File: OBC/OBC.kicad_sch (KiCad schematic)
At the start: 15 parts, among them J101 Modos de operación, J102 PMS-Raspi, J103 Conector UART, J104 Raspi-TRU, U101 RASPBERRY_PI_ZERO_2_W, U102 BMP280, U103 MPU9250

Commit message: Propone disposicion pcb
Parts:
- J103: footprint Connector_JST:JST_XH_S3B-XH-A-1_1x03_P2.50mm_Horizontal -> Connector_PinHeader_2.54mm:PinHeader_1x03_P2.54mm_Vertical
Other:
- sheet ADS1115_ADC ports: added +3.3v; removed +5V
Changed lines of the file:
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@@
 			)
 		)
-		(property "Footprint" "Connector_JST:JST_XH_S3B-XH-A-1_1x03_P2.50mm_Horizontal"
+		(property "Footprint" "Connector_PinHeader_2.54mm:PinHeader_1x03_P2.54mm_Vertical"
 			(at 245.11 107.95 0)
 			(effects
@@
 			)
 		)
-		(pin "+5V" input
+		(pin "+3.3v" input
 			(at 240.03 55.88 180)
 			(effects

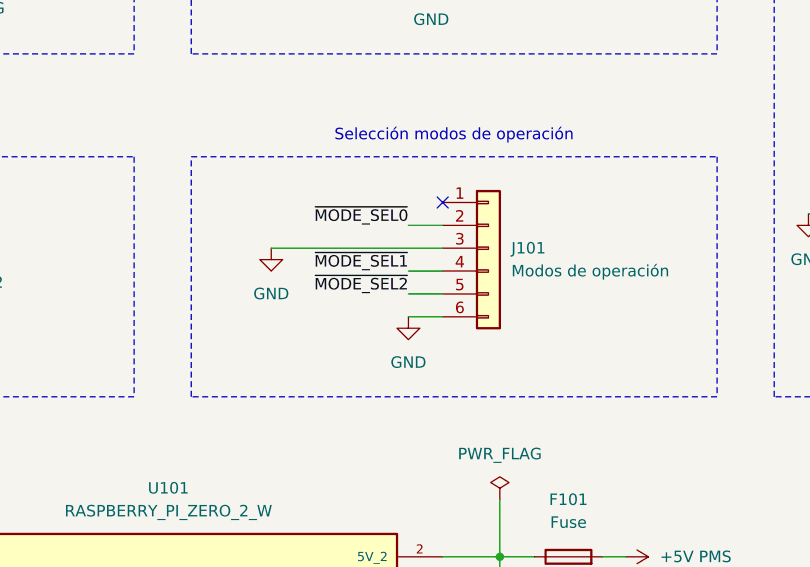
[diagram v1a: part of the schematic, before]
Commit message: Cambia disposición del selector de modos
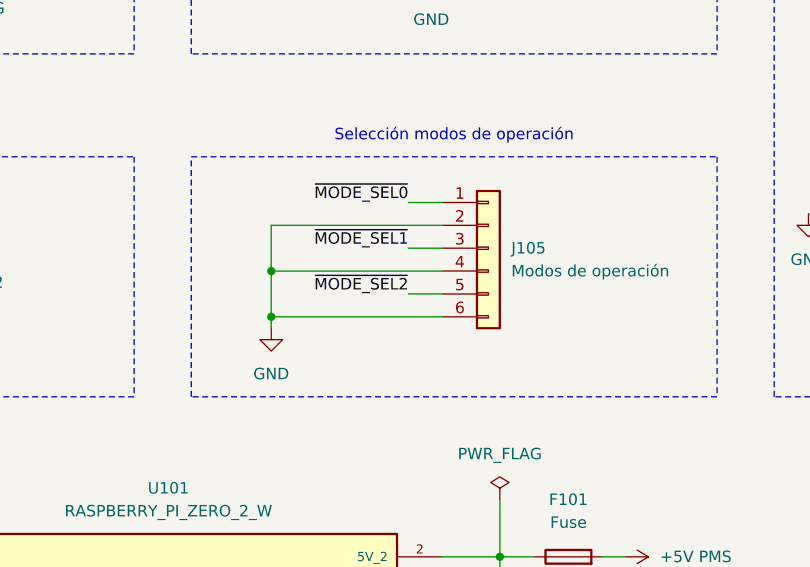
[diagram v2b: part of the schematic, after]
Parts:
- removed J101: Modos de operación, Connector_JST:JST_XH_S6B-XH-A_1x06_P2.50mm_Horizontal, symbol Connector_Generic:Conn_01x06
- added J105: Modos de operación, Connector_JST:JST_XH_S6B-XH-A_1x06_P2.50mm_Horizontal, symbol Connector_Generic:Conn_01x06
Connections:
- net GND: now also J105.2 (Pin_2), J105.4 (Pin_4), J105.6 (Pin_6)
- net ~{MODE_SEL0}: now also J105.1 (Pin_1)
- net ~{MODE_SEL1}: now also J105.3 (Pin_3)
- net ~{MODE_SEL2}: now also J105.5 (Pin_5)
- no-connect marks 38 -> 37

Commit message: Revisión v1.0
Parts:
- removed R106: 10k, Resistor_SMD:R_0603_1608Metric, symbol Device:R_Small
- R103, R104, R105: value 10k -> R
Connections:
- net +5V PMS: now also J104.6 (Pin_6); no longer J104.5 (Pin_5)
- net GND: now also U101.14 (GND_14), U101.20 (GND_20), U101.25 (GND_25), U101.30 (GND_30), U101.34 (GND_34), U101.39 (GND_39), U101.9 (GND_9); no longer J104.6 (Pin_6)
- net ~{MODE_SEL0}: now also J105.5 (Pin_5); no longer J105.1 (Pin_1)
- net ~{MODE_SEL2}: now also J105.1 (Pin_1); no longer J105.5 (Pin_5)
- net at C101.1, F101.1, U101.2 (5V_2): now also U101.4 (5V_4)
- net AIN3: no longer names the net of J104.4 (Pin_4)
- no-connect marks 37 -> 32
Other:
- company: (none) -> Team Corex
- title: (none) -> On Board Computer

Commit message: Correcciones menores
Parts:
- renumbered J102 to J101, J104 to J102, J105 to J103, J103 to J104, R105 to R101, R103 to R102, R104 to R103, R101 to R104, R102 to R105, U103 to U101, U101 to U103
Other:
- sheet ADS1115_ADC ports: added +3.3V; removed +3.3v
- company: Team Corex -> Team COREX
- title: On Board Computer -> Computadora a Bordo (OBC)

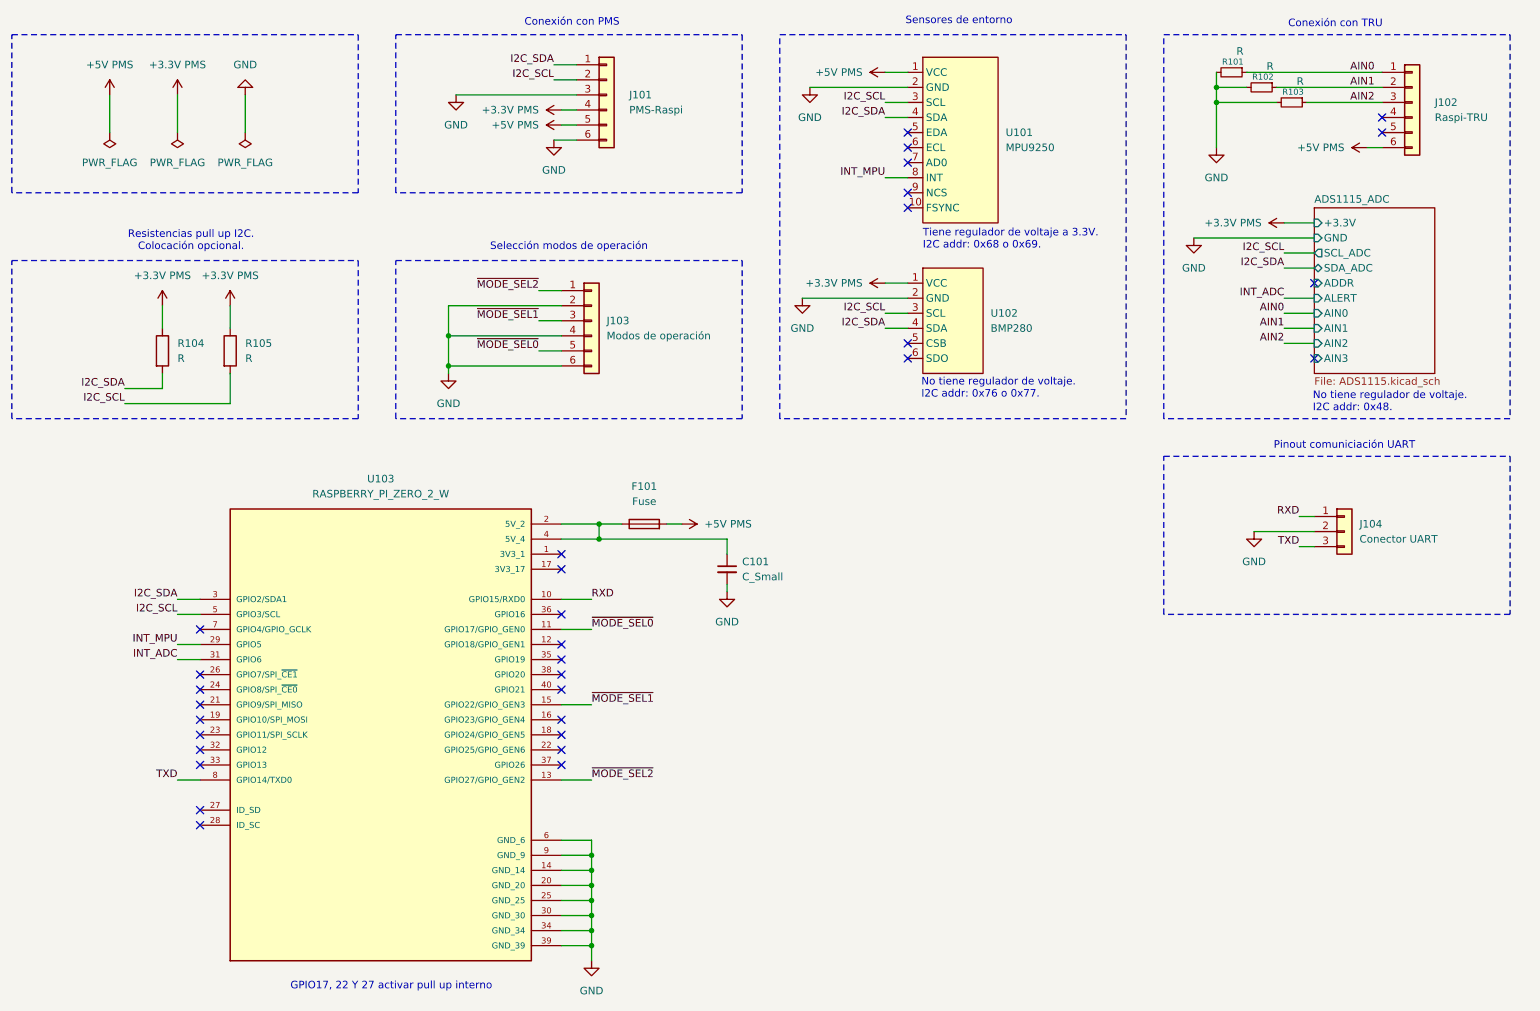
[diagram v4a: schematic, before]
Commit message: Remueve hmi fisico del obs y renombra componentes
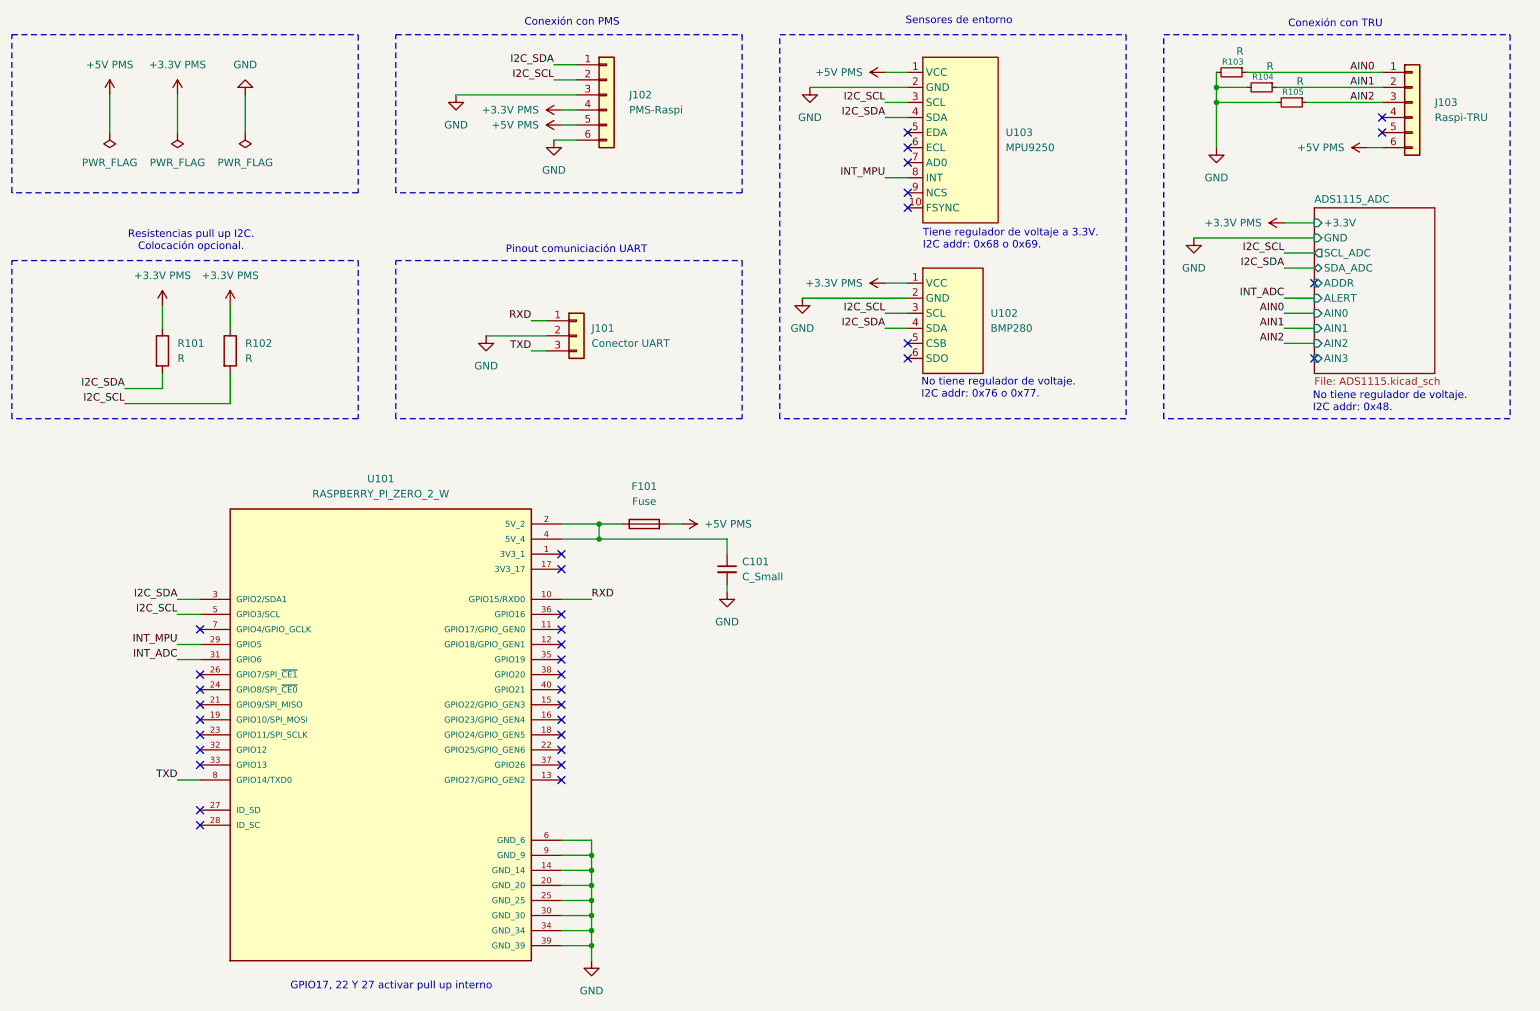
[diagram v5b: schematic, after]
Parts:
- removed J103: Modos de operación, Connector_JST:JST_XH_S6B-XH-A_1x06_P2.50mm_Horizontal, symbol Connector_Generic:Conn_01x06
- renumbered J104 to J101, J101 to J102, J102 to J103, R104 to R101, R105 to R102, R101 to R103, R102 to R104, R103 to R105, U103 to U101, U101 to U103
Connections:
- net ~{MODE_SEL0}: no longer names the net of U101.11 (GPIO17/GPIO_GEN0)
- net ~{MODE_SEL1}: no longer names the net of U101.15 (GPIO22/GPIO_GEN3)
- net ~{MODE_SEL2}: no longer names the net of U101.13 (GPIO27/GPIO_GEN2)
- no-connect marks 32 -> 35
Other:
- note removed: "Selección modos de operación"
- moved on the sheet: J101
